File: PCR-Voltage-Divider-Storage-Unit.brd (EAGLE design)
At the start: 88.9 x 94.9 mm, 100 parts

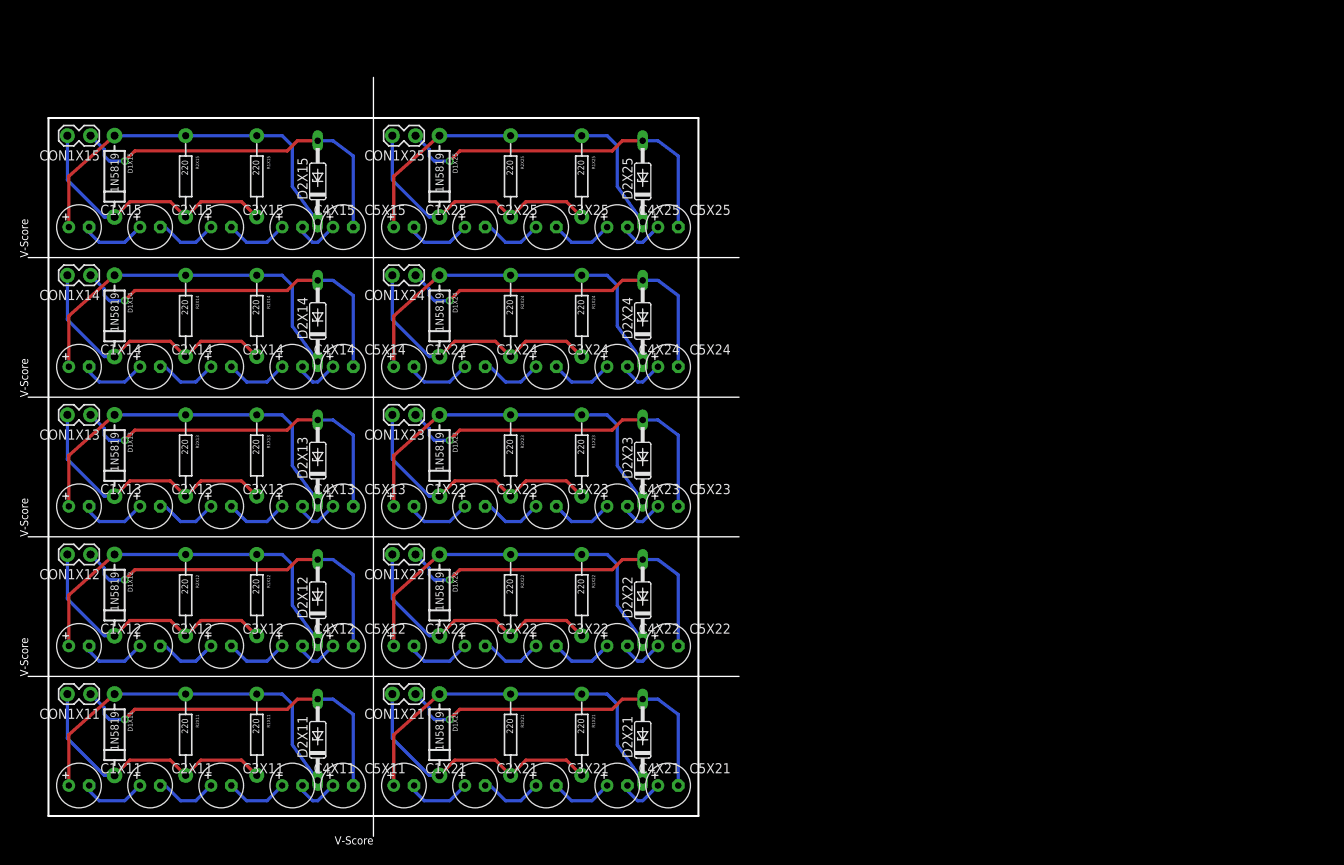
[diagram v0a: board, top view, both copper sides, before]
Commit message: first pass design is out for review
voltage divider capacitive storage device.  Just schematic capture and basic board layout.  I'll add labels before I send it out for fab.  My concern is that it's 55 mm long, so it will have to go 5 up.  I'd like to squeeze it down to 50mm
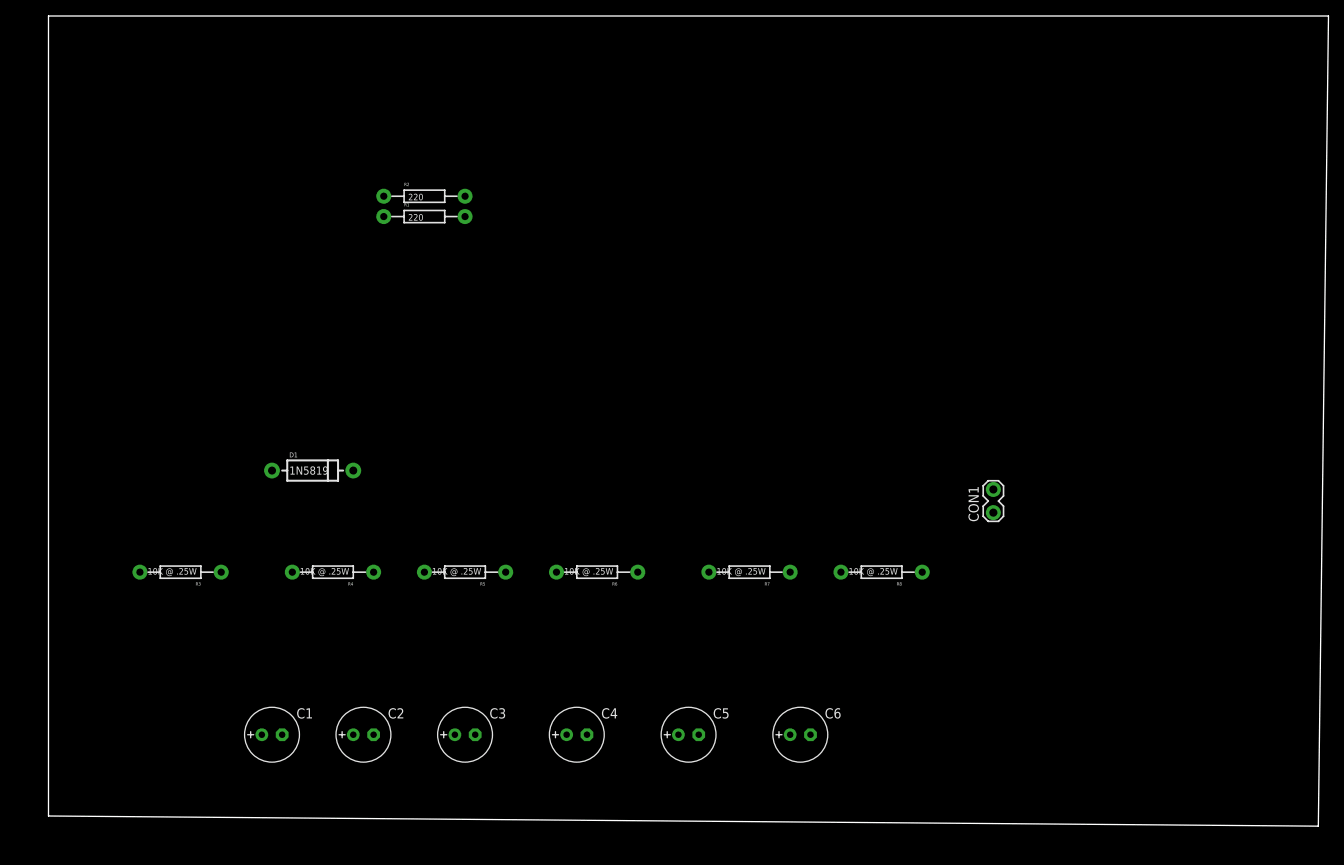
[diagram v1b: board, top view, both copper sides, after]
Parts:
- removed C1X11, C1X12, C1X13, C1X14, C1X15, C1X21, C1X22, C1X23, C1X24, C1X25, C2X11, C2X12, C2X13, C2X14, C2X15, C2X21, C2X22, C2X23, C2X24, C2X25, C3X11, C3X12, C3X13, C3X14, C3X15, C3X21, C3X22, C3X23, C3X24, C3X25, C4X11, C4X12, C4X13, C4X14, C4X15, C4X21, C4X22, C4X23, C4X24, C4X25, C5X11, C5X12, C5X13, C5X14, C5X15, C5X21, C5X22, C5X23, C5X24, C5X25: 1F @ 2.7V, rcl:E2,5-6
- removed CON1X11, CON1X12, CON1X13, CON1X14, CON1X15, CON1X21, CON1X22, CON1X23, CON1X24, CON1X25: (no value), SPCoast:1X02_LOCK
- removed D1X11, D1X12, D1X13, D1X14, D1X15, D1X21, D1X22, D1X23, D1X24, D1X25: 1N5819, SPCoast:DIODE-1N4001
- removed D2X11, D2X12, D2X13, D2X14, D2X15, D2X21, D2X22, D2X23, D2X24, D2X25: 1N5243B, diode:DO35Z10
- removed R1X11, R1X12, R1X13, R1X14, R1X15, R1X21, R1X22, R1X23, R1X24, R1X25, R2X11, R2X12, R2X13, R2X14, R2X15, R2X21, R2X22, R2X23, R2X24, R2X25: 220, SPCoast:AXIAL-0.4-RES
- added C1, C2, C3, C4, C5, C6: .22F @ 2.5V, rcl:E2,5-7
- added CON1: (no value), SPCoast:1X02_LOCK
- added D1: 1N5819, SPCoast:DIODE-1N4001
- added R1, R2: 220, SPCoast:AXIAL-0.4-RES
- added R3, R4, R5, R6, R7, R8: 10K @ .25W, SPCoast:AXIAL-0.4-RES
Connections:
- removed net N$1X11: C1X11.-, C2X11.+
- removed net N$1X12: C1X12.-, C2X12.+
- removed net N$1X13: C1X13.-, C2X13.+
- removed net N$1X14: C1X14.-, C2X14.+
- removed net N$1X15: C1X15.-, C2X15.+
- removed net N$1X21: C1X21.-, C2X21.+
- removed net N$1X22: C1X22.-, C2X22.+
- removed net N$1X23: C1X23.-, C2X23.+
- removed net N$1X24: C1X24.-, C2X24.+
- removed net N$1X25: C1X25.-, C2X25.+
- removed net N$2X11: C2X11.-, C3X11.+
- removed net N$2X12: C2X12.-, C3X12.+
- removed net N$2X13: C2X13.-, C3X13.+
- removed net N$2X14: C2X14.-, C3X14.+
- removed net N$2X15: C2X15.-, C3X15.+
- removed net N$2X21: C2X21.-, C3X21.+
- removed net N$2X22: C2X22.-, C3X22.+
- removed net N$2X23: C2X23.-, C3X23.+
- removed net N$2X24: C2X24.-, C3X24.+
- removed net N$2X25: C2X25.-, C3X25.+
- removed net N$3X11: C3X11.-, C4X11.+
- removed net N$3X12: C3X12.-, C4X12.+
- removed net N$3X13: C3X13.-, C4X13.+
- removed net N$3X14: C3X14.-, C4X14.+
- removed net N$3X15: C3X15.-, C4X15.+
- removed net N$3X21: C3X21.-, C4X21.+
- removed net N$3X22: C3X22.-, C4X22.+
- removed net N$3X23: C3X23.-, C4X23.+
- removed net N$3X24: C3X24.-, C4X24.+
- removed net N$3X25: C3X25.-, C4X25.+
- removed net N$4X11: C4X11.-, C5X11.+
- removed net N$4X12: C4X12.-, C5X12.+
- removed net N$4X13: C4X13.-, C5X13.+
- removed net N$4X14: C4X14.-, C5X14.+
- removed net N$4X15: C4X15.-, C5X15.+
- removed net N$4X21: C4X21.-, C5X21.+
- removed net N$4X22: C4X22.-, C5X22.+
- removed net N$4X23: C4X23.-, C5X23.+
- removed net N$4X24: C4X24.-, C5X24.+
- removed net N$4X25: C4X25.-, C5X25.+
- removed net N$6X11: C1X11.+, D1X11.A, D2X11.C, R1X11.P$1, R2X11.P$1
- removed net N$6X12: C1X12.+, D1X12.A, D2X12.C, R1X12.P$1, R2X12.P$1
- removed net N$6X13: C1X13.+, D1X13.A, D2X13.C, R1X13.P$1, R2X13.P$1
- removed net N$6X14: C1X14.+, D1X14.A, D2X14.C, R1X14.P$1, R2X14.P$1
- removed net N$6X15: C1X15.+, D1X15.A, D2X15.C, R1X15.P$1, R2X15.P$1
- removed net N$6X21: C1X21.+, D1X21.A, D2X21.C, R1X21.P$1, R2X21.P$1
- removed net N$6X22: C1X22.+, D1X22.A, D2X22.C, R1X22.P$1, R2X22.P$1
- removed net N$6X23: C1X23.+, D1X23.A, D2X23.C, R1X23.P$1, R2X23.P$1
- removed net N$6X24: C1X24.+, D1X24.A, D2X24.C, R1X24.P$1, R2X24.P$1
- removed net N$6X25: C1X25.+, D1X25.A, D2X25.C, R1X25.P$1, R2X25.P$1
- removed net NEGX11: C5X11.-, CON1X11.1, D2X11.A
- removed net NEGX12: C5X12.-, CON1X12.1, D2X12.A
- removed net NEGX13: C5X13.-, CON1X13.1, D2X13.A
- removed net NEGX14: C5X14.-, CON1X14.1, D2X14.A
- removed net NEGX15: C5X15.-, CON1X15.1, D2X15.A
- removed net NEGX21: C5X21.-, CON1X21.1, D2X21.A
- removed net NEGX22: C5X22.-, CON1X22.1, D2X22.A
- removed net NEGX23: C5X23.-, CON1X23.1, D2X23.A
- removed net NEGX24: C5X24.-, CON1X24.1, D2X24.A
- removed net NEGX25: C5X25.-, CON1X25.1, D2X25.A
- removed net POSX11: CON1X11.2, D1X11.C, R1X11.P$2, R2X11.P$2
- removed net POSX12: CON1X12.2, D1X12.C, R1X12.P$2, R2X12.P$2
- removed net POSX13: CON1X13.2, D1X13.C, R1X13.P$2, R2X13.P$2
- removed net POSX14: CON1X14.2, D1X14.C, R1X14.P$2, R2X14.P$2
- removed net POSX15: CON1X15.2, D1X15.C, R1X15.P$2, R2X15.P$2
- removed net POSX21: CON1X21.2, D1X21.C, R1X21.P$2, R2X21.P$2
- removed net POSX22: CON1X22.2, D1X22.C, R1X22.P$2, R2X22.P$2
- removed net POSX23: CON1X23.2, D1X23.C, R1X23.P$2, R2X23.P$2
- removed net POSX24: CON1X24.2, D1X24.C, R1X24.P$2, R2X24.P$2
- removed net POSX25: CON1X25.2, D1X25.C, R1X25.P$2, R2X25.P$2
- new net N$1: C1.-, C2.+, R3.P$1, R4.P$2
- new net N$2: C2.-, C3.+, R4.P$1, R5.P$2
- new net N$4: C4.-, C5.+, R6.P$1, R7.P$2
- new net N$5: C5.-, C6.+, R7.P$1, R8.P$2
- new net N$6: C1.+, D1.A, R1.P$1, R2.P$1, R3.P$2
- new net N$9: C3.-, C4.+, R5.P$1, R6.P$2
- new net NEG: C6.-, CON1.1, R8.P$1
- new net POS: CON1.2, D1.C, R1.P$2, R2.P$2
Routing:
- net N$6X23: track 47.3 -> 0.00 mm
- net N$6X25: track 47.3 -> 0.00 mm
- net N$6X24: track 47.3 -> 0.00 mm
- net N$6X21: track 47.3 -> 0.00 mm
- net N$6X15: track 47.3 -> 0.00 mm
- net N$6X14: track 47.3 -> 0.00 mm
- net N$6X11: track 47.3 -> 0.00 mm
- net N$6X22: track 47.3 -> 0.00 mm
- net N$6X13: track 47.3 -> 0.00 mm
- net N$6X12: track 47.3 -> 0.00 mm
- net NEGX15: track 45.2 -> 0.00 mm, vias 1 -> 0
- net NEGX25: track 45.2 -> 0.00 mm, vias 1 -> 0
- net NEGX23: track 45.2 -> 0.00 mm, vias 1 -> 0
- net NEGX11: track 45.2 -> 0.00 mm, vias 1 -> 0
- net NEGX22: track 45.2 -> 0.00 mm, vias 1 -> 0
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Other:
- board size 88.9 x 94.9 mm -> 160 x 101.3 mm
- board text removed: "- +"
- board text removed: "C1"
- board text removed: "C2"
- board text removed: "C3"
- board text removed: "C4"
- board text removed: "C5"
- board text removed: "CON1"
- board text removed: "D1"
- board text removed: "D2"
- board text removed: "PCR Keep Alive Version 1.0 Seth Neumann July 20. 2020"
- board text removed: "R1"
- board text removed: "R2"
- board text removed: "V-Score"
